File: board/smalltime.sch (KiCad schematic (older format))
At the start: 4 parts

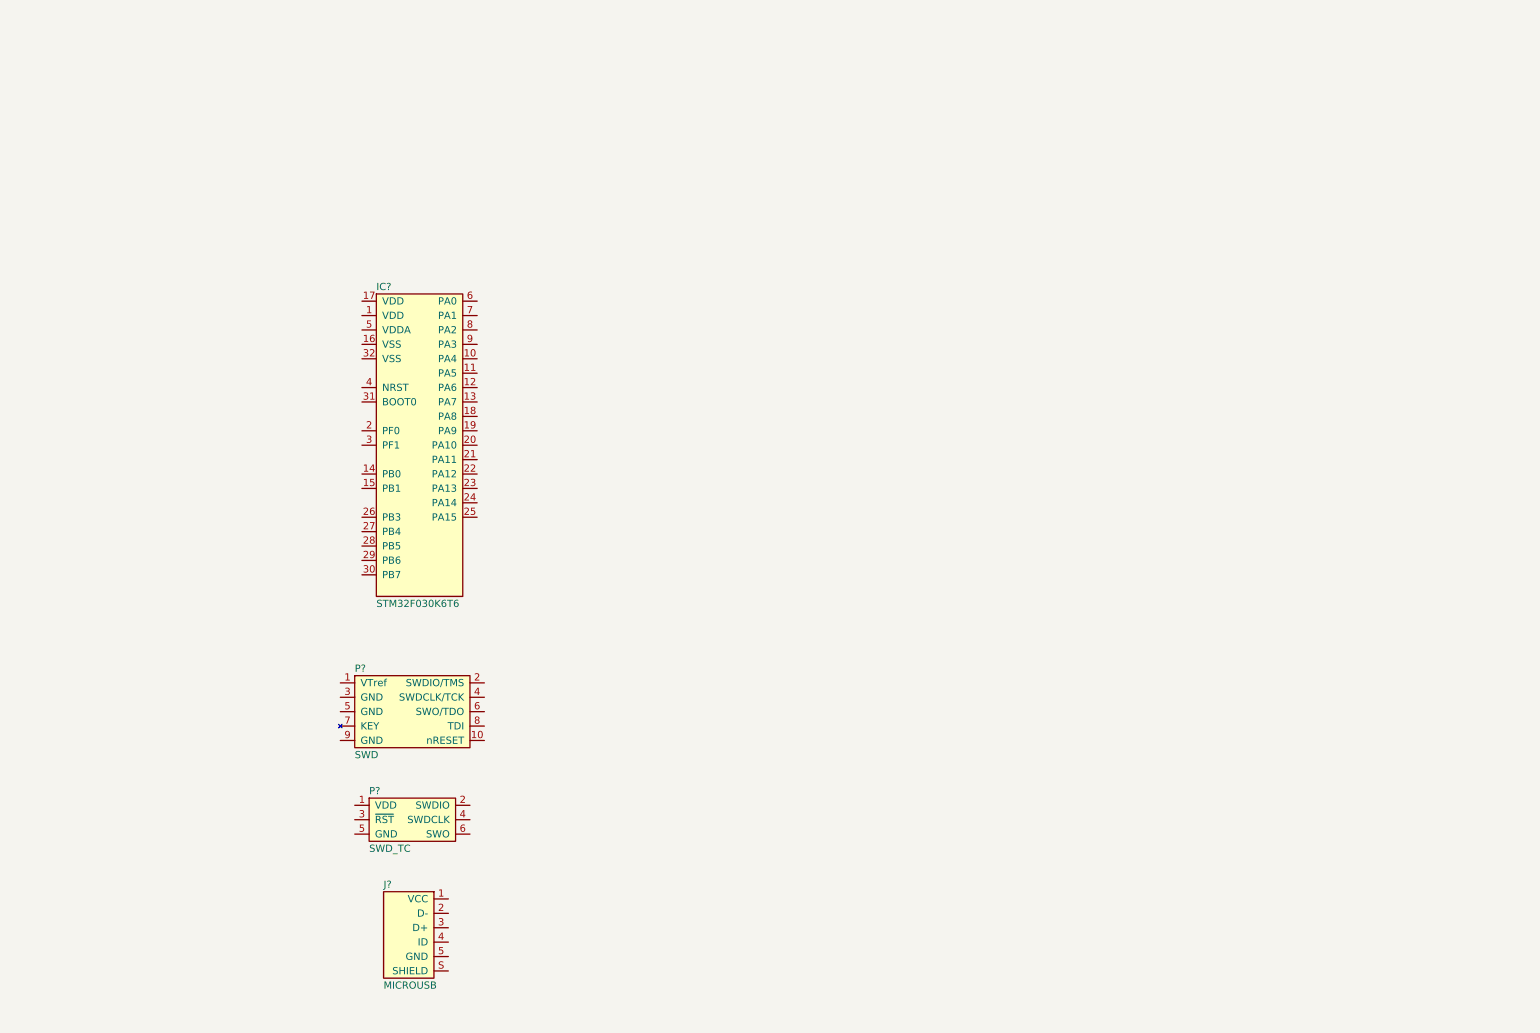
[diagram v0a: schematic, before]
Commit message: Added all parts to schematic
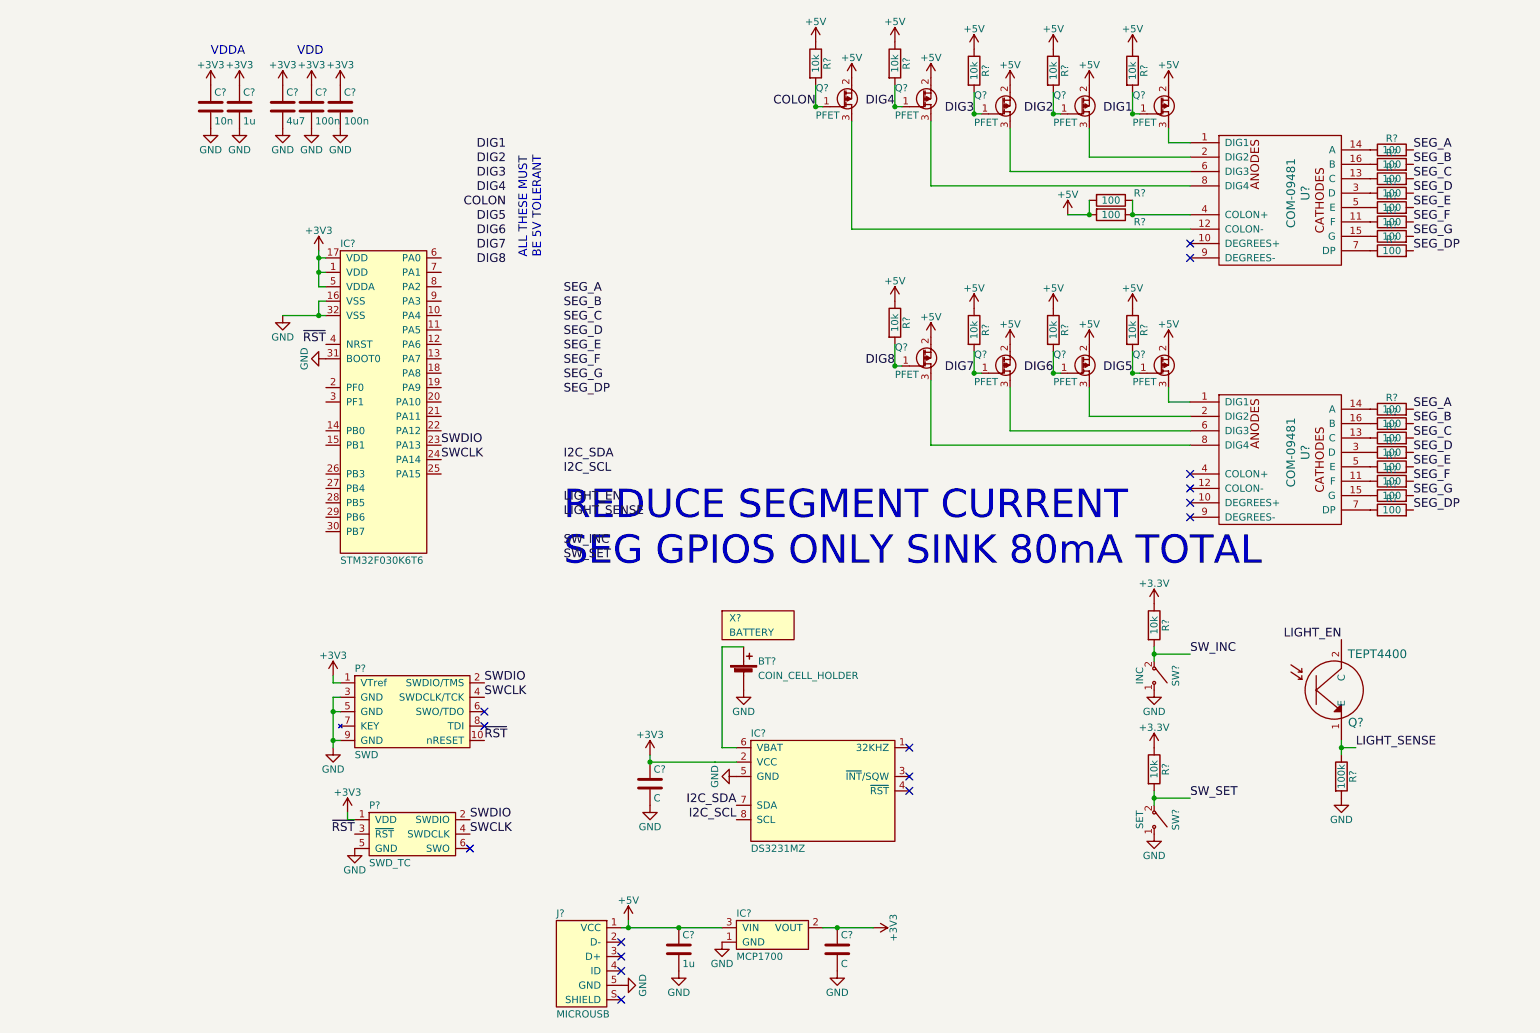
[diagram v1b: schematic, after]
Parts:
- added BT?: COIN_CELL_HOLDER, smalltime:2032HOLDER_KS1060, symbol Battery_Cell
- added C? (x2): C, symbol C
- added C?: 10n, symbol C
- added C? (x2): 1u, symbol C
- added C?: 4u7, symbol C
- added C? (x2): 100n, symbol C
- added IC?: DS3231MZ, agg:SOIC-8, symbol DS3231MZ
- added IC?: MCP1700, agg:SOT-23, symbol MCP1700
- added Q? (x9): PFET, agg:SOT-23, symbol PFET
- added Q?: TEPT4400, LEDs:LED_D3.0mm, symbol TEPT
- added R? (x11): 10k, agg:0603, symbol R
- added R?: 100k, agg:0603, symbol R
- added R? (x18): 100, agg:0603, symbol R
- added SW?: INC, symbol SWITCH_SPST
- added SW?: SET, symbol SWITCH_SPST
- added U? (x2): COM-09481, symbol COM-09481
- added X?: BATTERY, symbol PART
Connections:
- net +3V3: now reaches IC?.1 (VDD)
- net +3V3: now also IC?.17 (VDD), IC?.5 (VDDA), P?.1 (VDD), P?.1 (VTref), C?.1, C?.1, C?.1, C?.1, C?.1, C?.1, C?.1, IC?.2 (VCC), IC?.2 (VOUT), R?.1, R?.1
- net GND: now reaches IC?.16 (VSS)
- net GND: now also IC?.31 (BOOT0), IC?.32 (VSS), J?.5 (GND), P?.3 (GND), P?.5 (GND), P?.5 (GND), P?.9 (GND), BT?.2 (-), C?.2, C?.2, C?.2, C?.2, C?.2, C?.2, C?.2, C?.2, IC?.1 (GND), IC?.5 (GND), R?.2, SW?.1 ("~"), SW?.1 ("~")
- net SWDIO: now reaches IC?.23 (PA13)
- net SWDIO: now also P?.2 (SWDIO), P?.2 (SWDIO/TMS)
- net SWCLK: now reaches IC?.24 (PA14)
- net SWCLK: now also P?.4 (SWDCLK), P?.4 (SWDCLK/TCK)
- net ~RST: now reaches IC?.4 (NRST)
- net ~RST: now also P?.10 (nRESET), P?.3 (~RST)
- net +5V: now reaches J?.1 (VCC)
- net +5V: now also C?.1, IC?.3 (VIN), Q?.2 (S), Q?.2 (S), Q?.2 (S), Q?.2 (S), Q?.2 (S), Q?.2 (S), Q?.2 (S), Q?.2 (S), Q?.2 (S), R?.1, R?.1, R?.1, R?.1, R?.1, R?.1, R?.1, R?.1, R?.1, R?.2, R?.2
- new net: BT?.1 (+), IC?.6 (VBAT)
- new net: Q?.3 (D), U?.1 (DIG1) (x2)
- new net: R?.1, U?.11 (F) (x2)
- new net: Q?.3 (D), U?.12 (COLON-)
- new net: R?.1, U?.13 (C) (x2)
- new net: R?.1, U?.14 (A) (x2)
- new net: R?.1, U?.15 (G) (x2)
- new net: R?.1, U?.16 (B) (x2)
- new net: Q?.3 (D), U?.2 (DIG2) (x2)
- new net: R?.1, U?.3 (D) (x2)
- new net: R?.1, R?.1, U?.4 (COLON+)
- new net: R?.1, U?.5 (E) (x2)
- new net: Q?.3 (D), U?.6 (DIG3) (x2)
- new net: R?.1, U?.7 (DP) (x2)
- new net: Q?.3 (D), U?.8 (DIG4) (x2)
- new net COLON: Q?.1 (G), R?.2
- new net DIG1: Q?.1 (G), R?.2
- new net DIG2: Q?.1 (G), R?.2
- new net DIG3: Q?.1 (G), R?.2
- new net DIG4: Q?.1 (G), R?.2
- new net DIG5: Q?.1 (G), R?.2
- new net DIG6: Q?.1 (G), R?.2
- new net DIG7: Q?.1 (G), R?.2
- new net DIG8: Q?.1 (G), R?.2
- new net I2C_SCL: IC?.8 (SCL)
- new net I2C_SDA: IC?.7 (SDA)
- new net LIGHT_EN: Q?.2 (C)
- new net LIGHT_SENSE: Q?.1 (E), R?.1
- new net SEG_A: R?.2, R?.2
- new net SEG_B: R?.2, R?.2
- new net SEG_C: R?.2, R?.2
- new net SEG_D: R?.2, R?.2
- new net SEG_DP: R?.2, R?.2
- new net SEG_E: R?.2, R?.2
- new net SEG_F: R?.2, R?.2
- new net SEG_G: R?.2, R?.2
- new net SW_INC: R?.2, SW?.2 ("~")
- new net SW_SET: R?.2, SW?.2 ("~")
- no-connect marks 0 -> 16
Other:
- note added: "ALL THESE MUST\nBE 5V TOLERANT"
- note added: "REDUCE SEGMENT CURRENT\nSEG GPIOS ONLY SINK 80mA TOTAL"
- note added: "VDD"
- note added: "VDDA"
- moved on the sheet: IC?, J?, P?

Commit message: Added values and order codes
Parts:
- removed C? (x2): C, symbol C
- removed C?: 100n, symbol C
- removed C?: 1u, symbol C
- removed R? (x17): 100, agg:0603, symbol R
- added C? (x2): 1u, agg:0603, symbol C
- added C? (x2): 100n, agg:0603, symbol C
- added R? (x17): 160, agg:0603, symbol R
- C?: footprint (none) -> agg:0603; Farnell (none) -> 1759102
- C?: footprint (none) -> agg:0603; Farnell (none) -> 1759399
- C?: footprint (none) -> agg:0603; Farnell (none) -> 2320811
- C?: footprint (none) -> agg:0603; Farnell (none) -> 2627427
- Q?: Farnell (none) -> SC12389
- R?: Farnell (none) -> 2447226
- R?: value 100 -> 160; Farnell 2447227 -> 2447260
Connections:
- net +3V3: now also C?.1, C?.1, C?.1
- net +5V: now also C?.1, R?.1, R?.1
- net GND: now also C?.2, C?.2, C?.2, C?.2
- net SEG_A: now also R?.2
- net SEG_B: now also R?.2, R?.2
- net SEG_C: now also R?.2, R?.2
- net SEG_D: now also R?.2, R?.2
- net SEG_DP: now also R?.2, R?.2
- net SEG_E: now also R?.2, R?.2
- net SEG_F: now also R?.2, R?.2
- net SEG_G: now also R?.2, R?.2
- net at U?.11 (F): now also R?.1 (x2)
- net at U?.13 (C): now also R?.1 (x2)
- net at U?.15 (G): now also R?.1 (x2)
- net at U?.16 (B): now also R?.1 (x2)
- net at U?.3 (D): now also R?.1 (x2)
- net at U?.4 (COLON+): now also R?.2, R?.2
- net at U?.5 (E): now also R?.1 (x2)
- net at U?.7 (DP): now also R?.1 (x2)
- net at U?.14 (A): now also R?.1
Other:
- note removed: "REDUCE SEGMENT CURRENT\nSEG GPIOS ONLY SINK 80mA TOTAL"

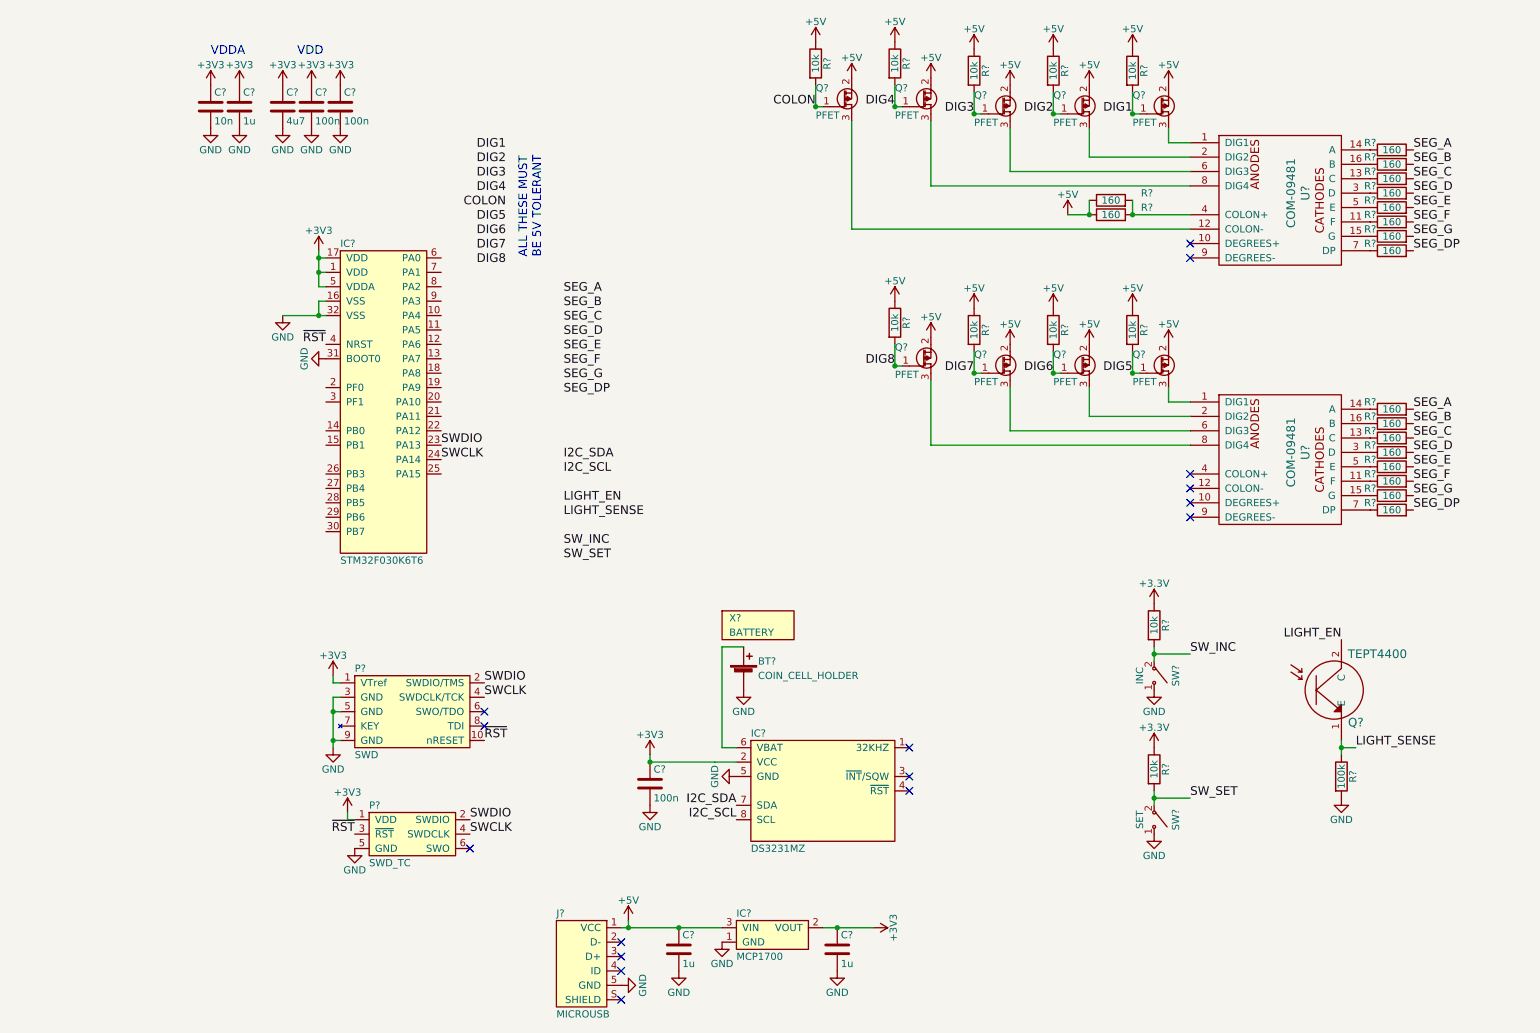
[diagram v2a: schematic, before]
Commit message: Added part number for push switches
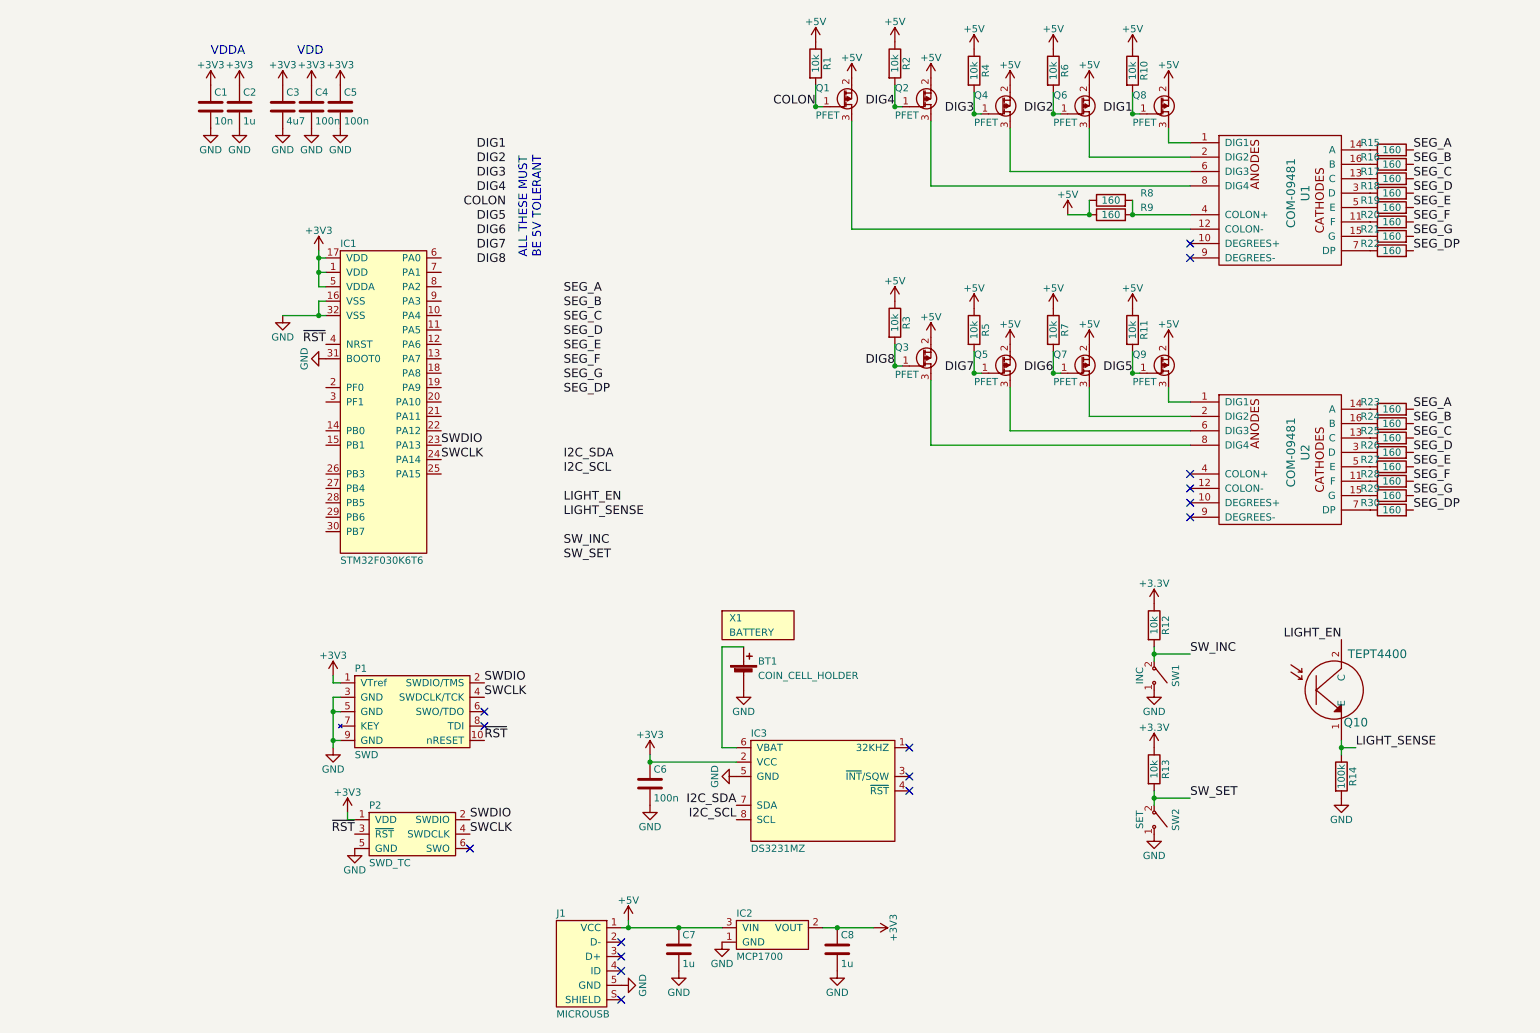
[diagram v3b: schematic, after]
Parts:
- SW1, SW2: renamed from SW?; Farnell (none) -> 2056829
- gave numbers to parts that had none: 58

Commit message: Added footprints for 7seg display and switches
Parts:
- SW1, SW2: footprint (none) -> smalltime:SKHHLSA010
- U1, U2: footprint (none) -> smalltime:YSD-439AB4B-35
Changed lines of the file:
@@
 F 0 "U1" V 9450 1750 60  0000 C CNN
 F 1 "COM-09481" V 9350 1750 60  0000 C CNN
-F 2 "" H 9550 1950 60  0001 C CNN
+F 2 "smalltime:YSD-439AB4B-35" H 9550 1950 60  0001 C CNN
 F 3 "https://www.sparkfun.com/datasheets/Components/LED/7-Segment/YSD-439AB4B-35.pdf" H 9550 1950 60  0001 C CNN
 	1    9350 1750
@@
 F 0 "U2" V 9450 3550 60  0000 C CNN
 F 1 "COM-09481" V 9350 3550 60  0000 C CNN
-F 2 "" H 9550 3750 60  0001 C CNN
+F 2 "smalltime:YSD-439AB4B-35" H 9550 3750 60  0001 C CNN
 F 3 "https://www.sparkfun.com/datasheets/Components/LED/7-Segment/YSD-439AB4B-35.pdf" H 9550 3750 60  0001 C CNN
 	1    9350 3550
@@
 F 0 "SW1" H 8400 5250 50  0000 C CNN
 F 1 "INC" H 8400 5000 50  0000 C CNN
-F 2 "" H 8400 5100 50  0001 C CNN
+F 2 "smalltime:SKHHLSA010" H 8400 5100 50  0001 C CNN
 F 3 "" H 8400 5100 50  0001 C CNN
 F 4 "2056829" H 8400 5100 60  0001 C CNN "Farnell"
@@
 F 0 "SW2" H 8400 6250 50  0000 C CNN
 F 1 "SET" H 8400 6000 50  0000 C CNN
-F 2 "" H 8400 6100 50  0001 C CNN
+F 2 "smalltime:SKHHLSA010" H 8400 6100 50  0001 C CNN
 F 3 "" H 8400 6100 50  0001 C CNN
 F 4 "2056829" H 8400 6100 60  0001 C CNN "Farnell"
